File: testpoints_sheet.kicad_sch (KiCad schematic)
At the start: 30 parts, among them J5 Conn_02x03_Odd_Even

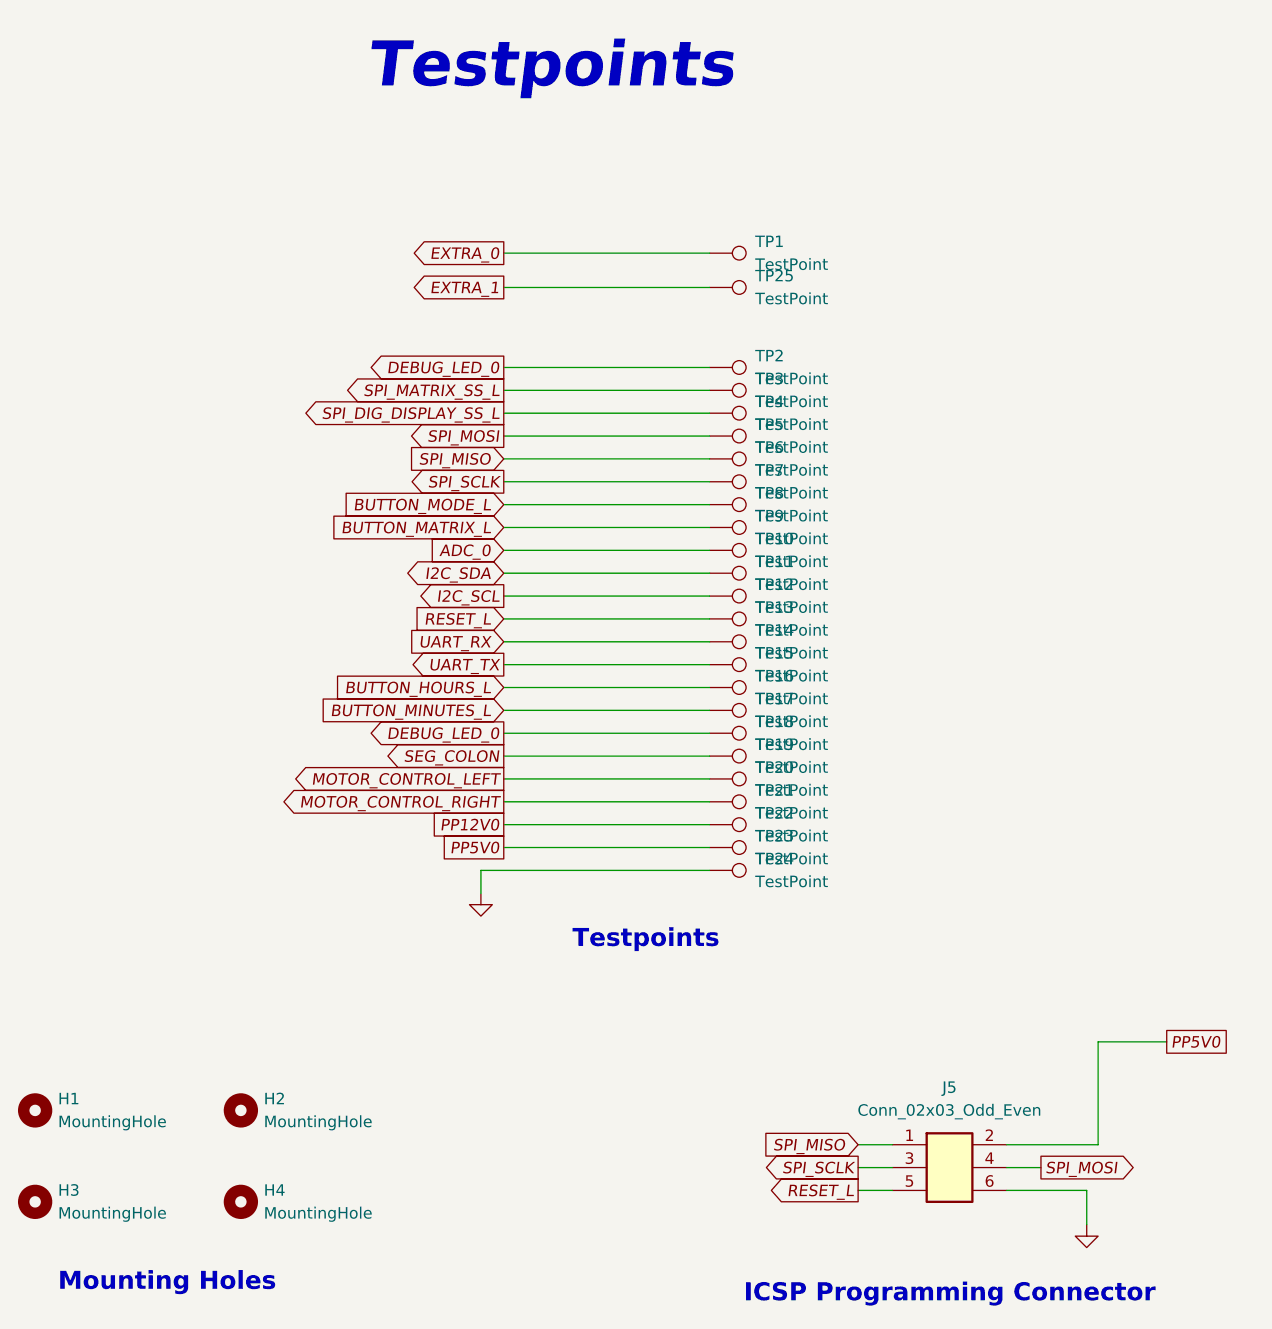
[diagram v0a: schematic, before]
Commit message: Initial gerber out
Got all of the files for gereber out
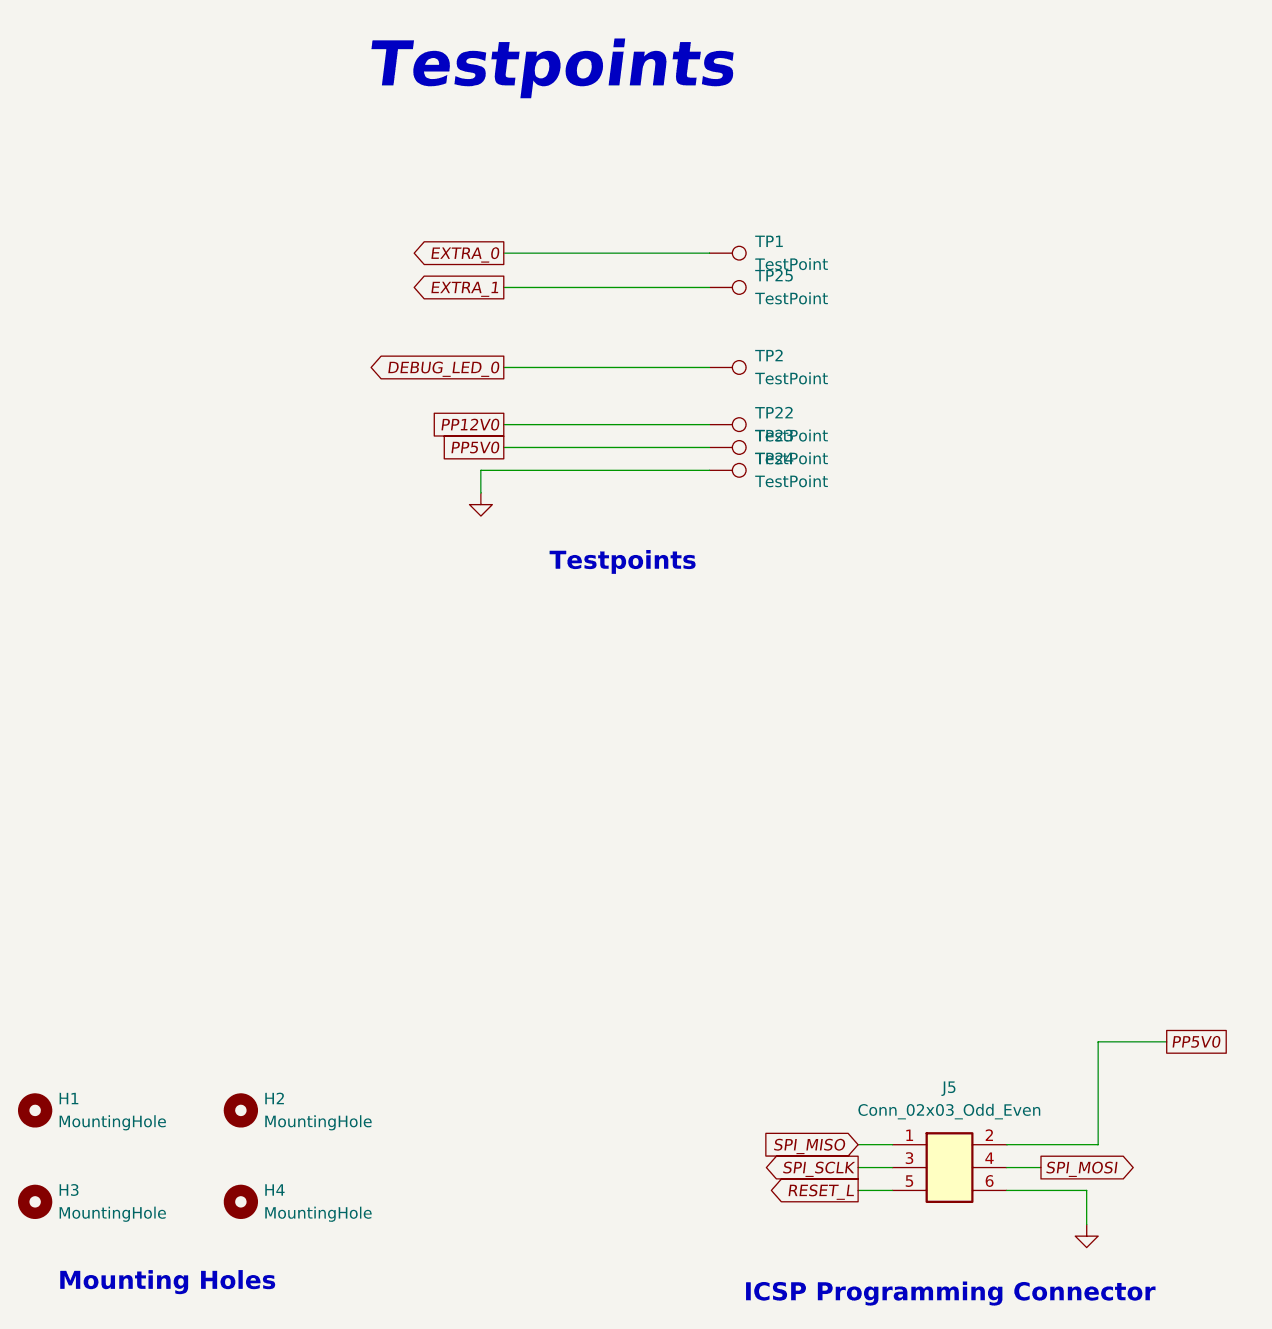
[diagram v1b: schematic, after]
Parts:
- removed TP10, TP11, TP12, TP13, TP14, TP15, TP16, TP17, TP18, TP19, TP20, TP21, TP3, TP4, TP5, TP6, TP7, TP8, TP9: TestPoint, footprints:TestPoint_THTPad_D2.0mm_Drill1.0mm, symbol HPS:TestPoint
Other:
- moved on the sheet: TP22, TP23, TP24
